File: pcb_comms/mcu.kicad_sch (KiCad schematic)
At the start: 29 parts, among them SW1 SW_SPDT, U3 STM32WLE5CCU6, Y1 32.768KHz, Y2 32MHz

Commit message: Last update
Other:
- company: (none) -> Sanie Peralta, Alejandro Campo
- title: (none) -> PC1: APRS & GPS
- moved on the sheet: C9, Y1
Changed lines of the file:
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@@
 	(generator_version "9.0")
 	(paper "A4")
-	(text "CLOCK\n"
+	(title_block
+		(title "PC1: APRS & GPS")
+		(date "2026-04-01")
+		(rev "1.0")
+		(company "Sanie Peralta, Alejandro Campo")
+		(comment 1 "Introducción a la Ingeniería Satelital ")
+		(comment 2 "Primer Parcial")
+	)
+	(text "RTC\n"
 		(exclude_from_sim no)
 		(at 46.99 83.82 0)
@@
 		)
 	)
-	(text "RTC\n"
+	(text "CLOCK\n"
 		(exclude_from_sim no)
 		(at 238.252 22.098 0)
@@
 		(exclude_from_sim no)
 		(at 20.955 80.01 0)
-		(size 53.34 29.21)
+		(size 53.34 31.115)
 		(margins 0.9525 0.9525 0.9525 0.9525)
 		(stroke
@@
 	)
 	(junction
-		(at 40.64 101.6)
+		(at 40.64 104.14)
 		(diameter 0)
 		(color 0 0 0 0)
@@
 	(wire
 		(pts
-			(xy 40.64 99.06) (xy 40.64 101.6)
+			(xy 40.64 100.33) (xy 40.64 104.14)
 		)
 		(stroke
@@
 	(wire
 		(pts
-			(xy 40.64 101.6) (xy 52.07 101.6)
+			(xy 40.64 104.14) (xy 52.07 104.14)
 		)
 		(stroke
@@
 	(wire
 		(pts
-			(xy 29.21 101.6) (xy 30.48 101.6)
+			(xy 29.21 104.14) (xy 30.48 104.14)
 		)
 		(stroke
@@
 	(wire
 		(pts
-			(xy 45.72 96.52) (xy 43.18 96.52)
+			(xy 43.18 97.79) (xy 45.72 97.79)
 		)
 		(stroke
@@
 	(wire
 		(pts
-			(xy 38.1 101.6) (xy 40.64 101.6)
+			(xy 38.1 104.14) (xy 40.64 104.14)
 		)
 		(stroke
@@
 	(wire
 		(pts
-			(xy 40.64 91.44) (xy 40.64 93.98)
+			(xy 40.64 91.44) (xy 40.64 95.25)
 		)
 		(stroke
@@
 	)
 	(label "STM32_OSC_RTC_OUT"
-		(at 52.07 101.6 0)
+		(at 52.07 104.14 0)
 		(effects
 			(font
@@
 	(symbol
 		(lib_id "Device:C")
-		(at 34.29 101.6 90)
+		(at 34.29 104.14 90)
 		(unit 1)
 		(exclude_from_sim no)
@@
 		(dnp no)
 		(property "Reference" "C9"
-			(at 34.29 98.552 90)
+			(at 31.75 105.41 90)
 			(effects
 				(font
@@
 		)
 		(property "Value" "6.8pF"
-			(at 34.29 105.41 90)
+			(at 38.354 105.664 90)
 			(effects
 				(font
@@
 		)
 		(property "Footprint" ""
-			(at 38.1 100.6348 0)
+			(at 38.1 103.1748 0)
 			(effects
 				(font
@@
 		)
 		(property "Datasheet" "~"
-			(at 34.29 101.6 0)
+			(at 34.29 104.14 0)
 			(effects
 				(font
@@
 		)
 		(property "Description" "Unpolarized capacitor"
-			(at 34.29 101.6 0)
+			(at 34.29 104.14 0)
 			(effects
 				(font
@@
 	(symbol
 		(lib_id "power:GND")
-		(at 29.21 101.6 270)
+		(at 29.21 104.14 270)
 		(unit 1)
 		(exclude_from_sim no)
@@
 		(dnp no)
 		(property "Reference" "#PWR013"
-			(at 22.86 101.6 0)
+			(at 22.86 104.14 0)
 			(effects
 				(font
@@
 		)
 		(property "Value" "GND"
-			(at 24.13 101.346 90)
+			(at 24.13 103.886 90)
 			(effects
 				(font
@@
 		)
 		(property "Footprint" ""
-			(at 29.21 101.6 0)
+			(at 29.21 104.14 0)
 			(effects
 				(font
@@
 		)
 		(property "Datasheet" ""
-			(at 29.21 101.6 0)
+			(at 29.21 104.14 0)
 			(effects
 				(font
@@
 		)
 		(property "Description" "Power symbol creates a global label with name \"GND\" , ground"
-			(at 29.21 101.6 0)
+			(at 29.21 104.14 0)
 			(effects
 				(font
@@
 		(dnp no)
 		(property "Reference" "C8"
-			(at 34.29 87.884 90)
+			(at 31.496 90.678 90)
 			(effects
 				(font
@@
 		)
 		(property "Value" "6.8pF"
-			(at 34.29 94.996 90)
+			(at 38.1 90.424 90)
 			(effects
 				(font
@@
 	(symbol
 		(lib_id "power:GND")
-		(at 45.72 96.52 90)
+		(at 45.72 97.79 90)
 		(unit 1)
 		(exclude_from_sim no)
@@
 		(dnp no)
 		(property "Reference" "#PWR09"
-			(at 52.07 96.52 0)
+			(at 52.07 97.79 0)
 			(effects
 				(font
@@
 		)
 		(property "Value" "GND"
-			(at 44.958 97.79 90)
+			(at 44.958 99.06 90)
 			(effects
 				(font
@@
 		)
 		(property "Footprint" ""
-			(at 45.72 96.52 0)
+			(at 45.72 97.79 0)
 			(effects
 				(font
@@
 		)
 		(property "Datasheet" ""
-			(at 45.72 96.52 0)
+			(at 45.72 97.79 0)
 			(effects
 				(font
@@
 		)
 		(property "Description" "Power symbol creates a global label with name \"GND\" , ground"
-			(at 45.72 96.52 0)
+			(at 45.72 97.79 0)
 			(effects
 				(font
@@
 	(symbol
 		(lib_id "Device:Crystal_GND24_Small")
-		(at 40.64 96.52 90)
+		(at 40.64 97.79 90)
 		(mirror x)
 		(unit 1)
@@
 		(dnp no)
 		(property "Reference" "Y1"
-			(at 39.116 93.726 90)
+			(at 39.116 94.996 90)
 			(effects
 				(font
@@
 		)
 		(property "Value" "32.768KHz"
-			(at 42.164 103.124 90)
+			(at 33.274 98.044 90)
 			(effects
 				(font
@@
 		)
 		(property "Footprint" ""
-			(at 40.64 96.52 0)
+			(at 40.64 97.79 0)
 			(effects
 				(font
@@
 		)
 		(property "Datasheet" "~"
-			(at 40.64 96.52 0)
+			(at 40.64 97.79 0)
 			(effects
 				(font
@@
 		)
 		(property "Description" "Four pin crystal, GND on pins 2 and 4, small symbol"
-			(at 40.64 96.52 0)
+			(at 40.64 97.79 0)
 			(effects
 				(font
@@
 		)
 		(property private "KLC_S3.3" "The rectangle is not a symbol body but a graphical element"
-			(at 50.8 96.52 0)
+			(at 50.8 97.79 0)
 			(show_name yes)
 			(effects
@@
 		)
 		(property private "KLC_S4.1" "Some pins are on 50mil grid to make the symbol small"
-			(at 53.34 96.52 0)
+			(at 53.34 97.79 0)
 			(show_name yes)
 			(effects

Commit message: rev 1.1
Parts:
- C6: value 4.7nF -> 4.7uF
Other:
- note added: "Capactiores cerca del STM32"
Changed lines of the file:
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@@
 		)
 	)
+	(text "Capactiores cerca \ndel STM32"
+		(exclude_from_sim no)
+		(at 88.392 174.752 0)
+		(effects
+			(font
+				(size 0.889 0.889)
+			)
+		)
+	)
 	(text "CLOCK\n"
 		(exclude_from_sim no)
@@
 		(exclude_from_sim no)
 		(at 19.05 161.29 0)
-		(size 64.135 33.02)
+		(size 80.01 33.02)
 		(margins 0.9525 0.9525 0.9525 0.9525)
 		(stroke
@@
 		)
 	)
+	(text_box "\n"
+		(exclude_from_sim no)
+		(at 81.28 170.815 0)
+		(size 13.97 6.985)
+		(margins 0.9525 0.9525 0.9525 0.9525)
+		(stroke
+			(width 0)
+			(type solid)
+		)
+		(fill
+			(type none)
+		)
+		(effects
+			(font
+				(size 1.27 1.27)
+			)
+			(justify left top)
+		)
+	)
 	(junction
 		(at 54.61 26.67)
@@
 	)
 	(junction
+		(at 40.64 139.7)
+		(diameter 0)
+		(color 0 0 0 0)
+	)
+	(junction
 		(at 68.58 49.53)
 		(diameter 0)
@@
 	(wire
 		(pts
+			(xy 36.83 139.7) (xy 40.64 139.7)
+		)
+		(stroke
+			(width 0)
+			(type default)
+		)
+	)
+	(wire
+		(pts
 			(xy 25.4 52.07) (xy 35.56 52.07)
 		)
@@
 	(wire
 		(pts
+			(xy 40.64 139.7) (xy 40.64 143.51)
+		)
+		(stroke
+			(width 0)
+			(type default)
+		)
+	)
+	(wire
+		(pts
 			(xy 113.03 38.1) (xy 113.03 41.91)
 		)
@@
 	(wire
 		(pts
+			(xy 40.64 139.7) (xy 53.34 139.7)
+		)
+		(stroke
+			(width 0)
+			(type default)
+		)
+	)
+	(wire
+		(pts
 			(xy 25.4 25.4) (xy 25.4 26.67)
 		)
@@
 	(wire
 		(pts
-			(xy 40.64 140.97) (xy 53.34 140.97)
-		)
-		(stroke
-			(width 0)
-			(type default)
-		)
-	)
-	(wire
-		(pts
 			(xy 212.09 110.49) (xy 208.28 110.49)
 		)
@@
 	(wire
 		(pts
-			(xy 40.64 140.97) (xy 40.64 143.51)
+			(xy 46.99 129.54) (xy 50.8 129.54)
 		)
 		(stroke
@@
 	(wire
 		(pts
-			(xy 46.99 129.54) (xy 50.8 129.54)
+			(xy 208.28 130.81) (xy 227.33 130.81)
 		)
 		(stroke
@@
 	(wire
 		(pts
-			(xy 208.28 130.81) (xy 227.33 130.81)
+			(xy 212.09 107.95) (xy 208.28 107.95)
 		)
 		(stroke
@@
 	(wire
 		(pts
-			(xy 212.09 107.95) (xy 208.28 107.95)
+			(xy 208.28 113.03) (xy 227.33 113.03)
 		)
 		(stroke
@@
 	(wire
 		(pts
-			(xy 208.28 113.03) (xy 227.33 113.03)
+			(xy 53.34 140.97) (xy 53.34 139.7)
 		)
 		(stroke
@@
 	)
 	(label "STM32_NRST"
-		(at 53.34 140.97 180)
+		(at 36.83 139.7 180)
 		(effects
 			(font
@@
 			)
 		)
-		(property "Value" "4.7nF"
+		(property "Value" "4.7uF"
 			(at 52.832 67.564 0)
 			(effects

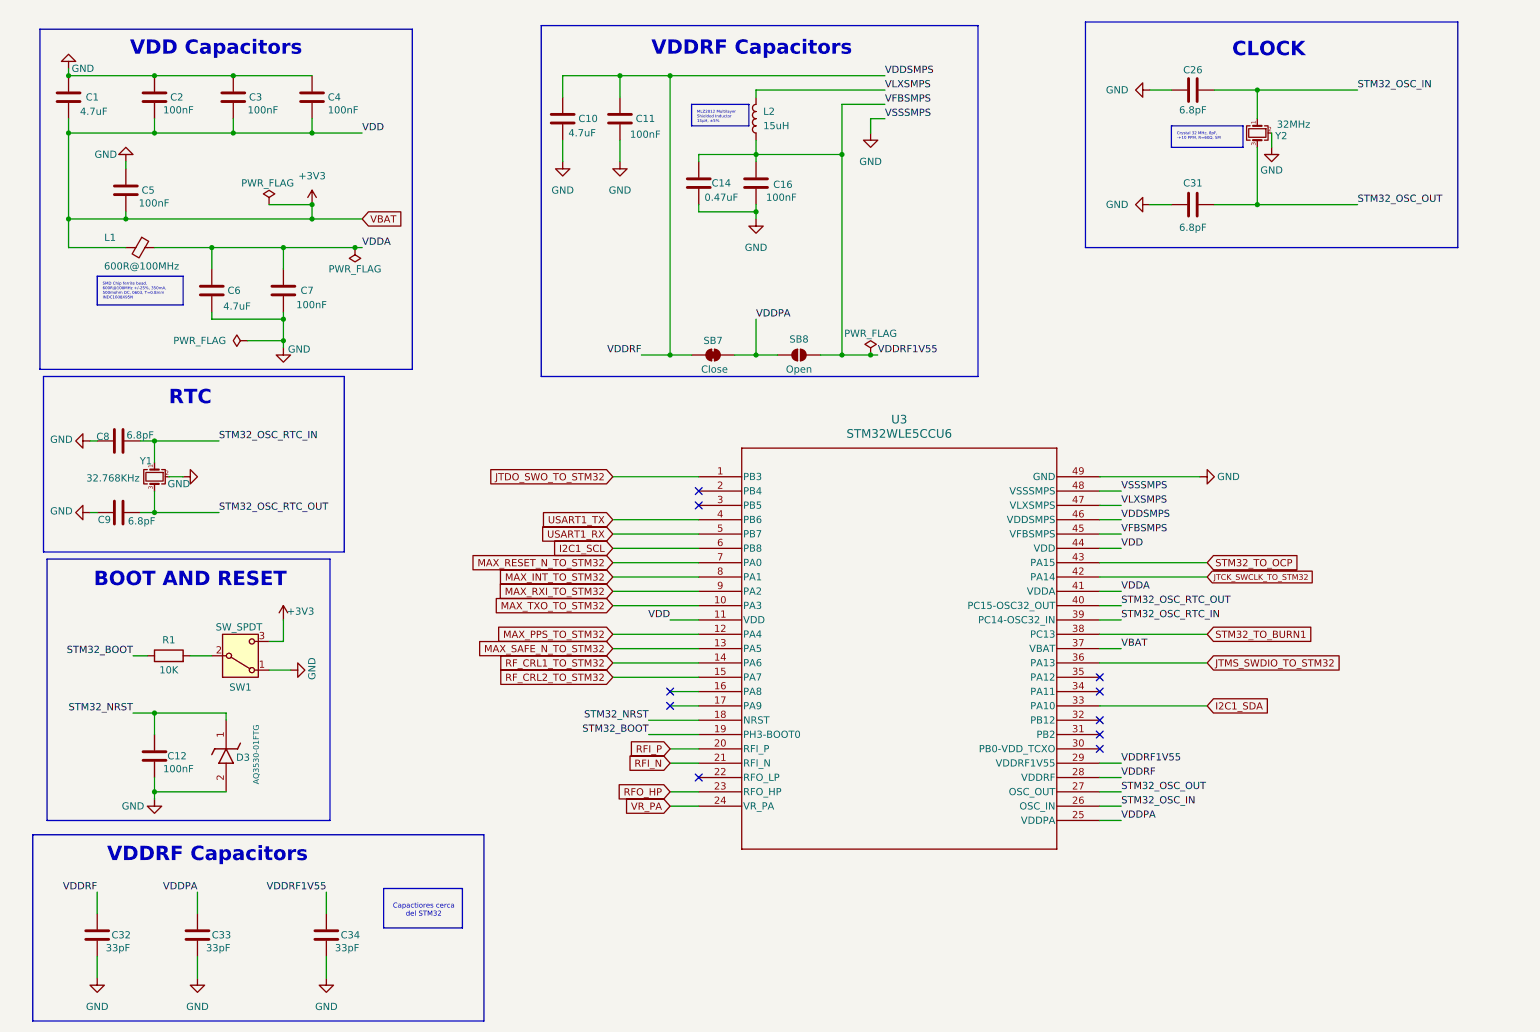
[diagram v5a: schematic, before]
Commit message: Finish schematic
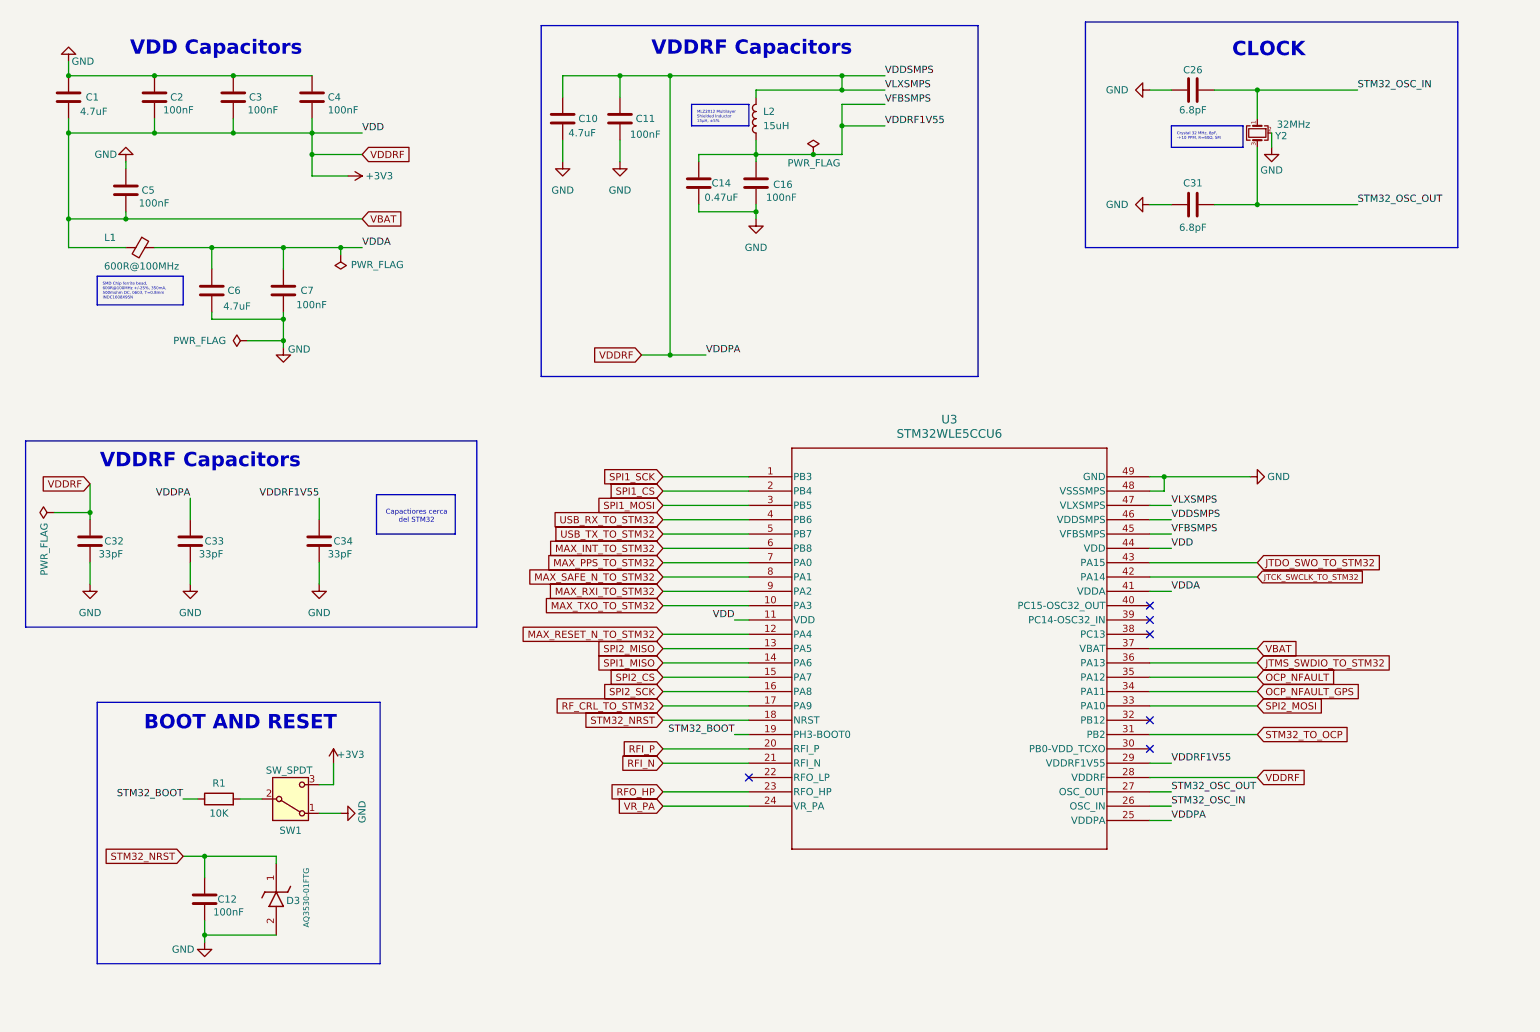
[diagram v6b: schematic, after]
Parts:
- removed C8, C9: 6.8pF, symbol Device:C
- removed SB7: Close, symbol Jumper:SolderJumper_2_Bridged
- removed SB8: Open, symbol Jumper:SolderJumper_2_Open
- removed Y1: 32.768KHz, symbol Device:Crystal_GND24_Small
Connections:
- net I2C1_SCL is gone; now on net MAX_INT_TO_STM32: U3.6 (PB8)
- net VDDPA is gone; now on net +3V3: C33.1, U3.25 (VDDPA)
- net VDDRF is gone; now on net +3V3: C10.1, C11.1, C32.1, U3.28 (VDDRF), U3.46 (VDDSMPS)
- net VLXSMPS is gone; now on net +3V3: L2.1, U3.47 (VLXSMPS)
- net JTDO_SWO_TO_STM32: now also U3.43 (PA15); no longer U3.1 (PB3)
- net MAX_INT_TO_STM32: no longer U3.8 (PA1)
- net MAX_PPS_TO_STM32: now also U3.7 (PA0); no longer U3.12 (PA4)
- net MAX_RESET_N_TO_STM32: now also U3.12 (PA4); no longer U3.7 (PA0)
- net MAX_SAFE_N_TO_STM32: now also U3.8 (PA1); no longer U3.13 (PA5)
- net STM32_TO_OCP: now also U3.31 (PB2); no longer U3.43 (PA15)
- net SPI2_SCK: now reaches U3.16 (PA8)
- net RF_CRL_TO_STM32: now reaches U3.17 (PA9)
- net SPI1_CS: now reaches U3.2 (PB4)
- net SPI1_MOSI: now reaches U3.3 (PB5)
- net OCP_NFAULT_GPS: now reaches U3.34 (PA11)
- net OCP_NFAULT: now reaches U3.35 (PA12)
- net I2C1_SDA renamed SPI2_MOSI
- net RF_CRL1_TO_STM32 renamed SPI1_MISO
- net RF_CRL2_TO_STM32 renamed SPI2_CS
- net STM32_OSC_RTC_IN: no longer names the net of U3.39 (PC14-OSC32_IN)
- net STM32_OSC_RTC_OUT: no longer names the net of U3.40 (PC15-OSC32_OUT)
- net STM32_TO_BURN1: no longer names the net of U3.38 (PC13)
- net USART1_RX renamed USB_TX_TO_STM32
- net USART1_TX renamed USB_RX_TO_STM32
- new net SPI1_SCK: U3.1 (PB3)
- new net SPI2_MISO: U3.13 (PA5)
- no-connect marks 10 -> 6
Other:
- note removed: "RTC"
- moved on the sheet: C12, C32, C33, C34, D3, R1, SW1, U3

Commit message: Version 1.0. No DRA yet
From now on I will make the connections for IIS and then adapt it for the club
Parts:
- removed U3: STM32WLE5CCU6, symbol STM32WL5:STM32WLE5CCU6
- removed Y2: 32MHz, symbol Device:Crystal_GND24_Small
- added U2: STM32WLE5CCU6, STM32WLE5:UFQFPN48_STM, symbol STM32WLE5:STM32WLE5CCU6
- added Y3: 32MHz, STM32WLE5_Crystal_32MHz:STM32WLE5_Crystal_32MHz_ECS320837CKMTR3, symbol STM32WLE5_Crystal_32MHz_ECS-320-8-37-CKM-TR3:ECS-320-8-37-CKM-TR3
- C11, C12, C16, C2, C3, C4, C5, C7: value 100nF -> 0.1uF
- L1: value 600R@100MHz -> 600R
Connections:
- net +3V3: now also U2.11 (VDD), U2.25 (VDDPA), U2.28 (VDDRF), U2.37 (VBAT), U2.44 (VDD), U2.46 (VDDSMPS), U2.47 (VLXSMPS)
- net GND: now also U2.48 (VSSSMPS), U2.49 (GND), Y3.2 (GND_1), Y3.4 (GND_2)
- net JTCK_SWCLK_TO_STM32: now also U2.42 (PA14)
- net JTDO_SWO_TO_STM32: now also U2.43 (PA15)
- net JTMS_SWDIO_TO_STM32: now also U2.36 (PA13)
- net MAX_INT_TO_STM32: now also U2.6 (PB8)
- net MAX_PPS_TO_STM32: now also U2.7 (PA0)
- net MAX_RESET_N_TO_STM32: now also U2.12 (PA4)
- net MAX_RXI_TO_STM32: now also U2.9 (PA2)
- net MAX_SAFE_N_TO_STM32: now also U2.8 (PA1)
- net MAX_TXO_TO_STM32: now also U2.10 (PA3)
- net OCP_NFAULT_GPS: now also U2.34 (PA11)
- net RFI_N: now also U2.21 (RFI_N)
- net RFI_P: now also U2.20 (RFI_P)
- net RFO_HP: now also U2.23 (RFO_HP)
- net RF_CRL_TO_STM32: now also U2.17 (PA9)
- net SPI1_CS: now also U2.2 (PB4)
- net SPI1_MISO: now also U2.14 (PA6)
- net SPI1_MOSI: now also U2.3 (PB5)
- net SPI1_SCK: now also U2.1 (PB3)
- net SPI2_CS: now also U2.15 (PA7)
- net SPI2_MISO: now also U2.13 (PA5)
- net SPI2_MOSI: now also U2.33 (PA10)
- net SPI2_SCK: now also U2.16 (PA8)
- net STM32_BOOT: now also U2.19 (PH3-BOOT0)
- net STM32_NRST: now also U2.18 (NRST)
- net STM32_OSC_IN: now also U2.26 (OSC_IN), Y3.1 (IN/OUT)
- net STM32_OSC_OUT: now also U2.27 (OSC_OUT), Y3.3 (OUT/IN)
- net STM32_TO_OCP: now also U2.31 (PB2)
- net USB_RX_TO_STM32: now also U2.4 (PB6)
- net USB_TX_TO_STM32: now also U2.5 (PB7)
- net VDDA: now also U2.41 (VDDA)
- net VDDRF1V55: now also U2.29 (VDDRF1V55), U2.45 (VFBSMPS)
- net VR_PA: now also U2.24 (VR_PA)
- no-connect marks 6 -> 7
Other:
- note added: "VDDRF Components"
- moved on the sheet: C26, C31
